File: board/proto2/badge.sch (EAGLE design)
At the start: 61 parts, among them IC1 TLV62569, J1 5051101092, J2 M05X2X1.27

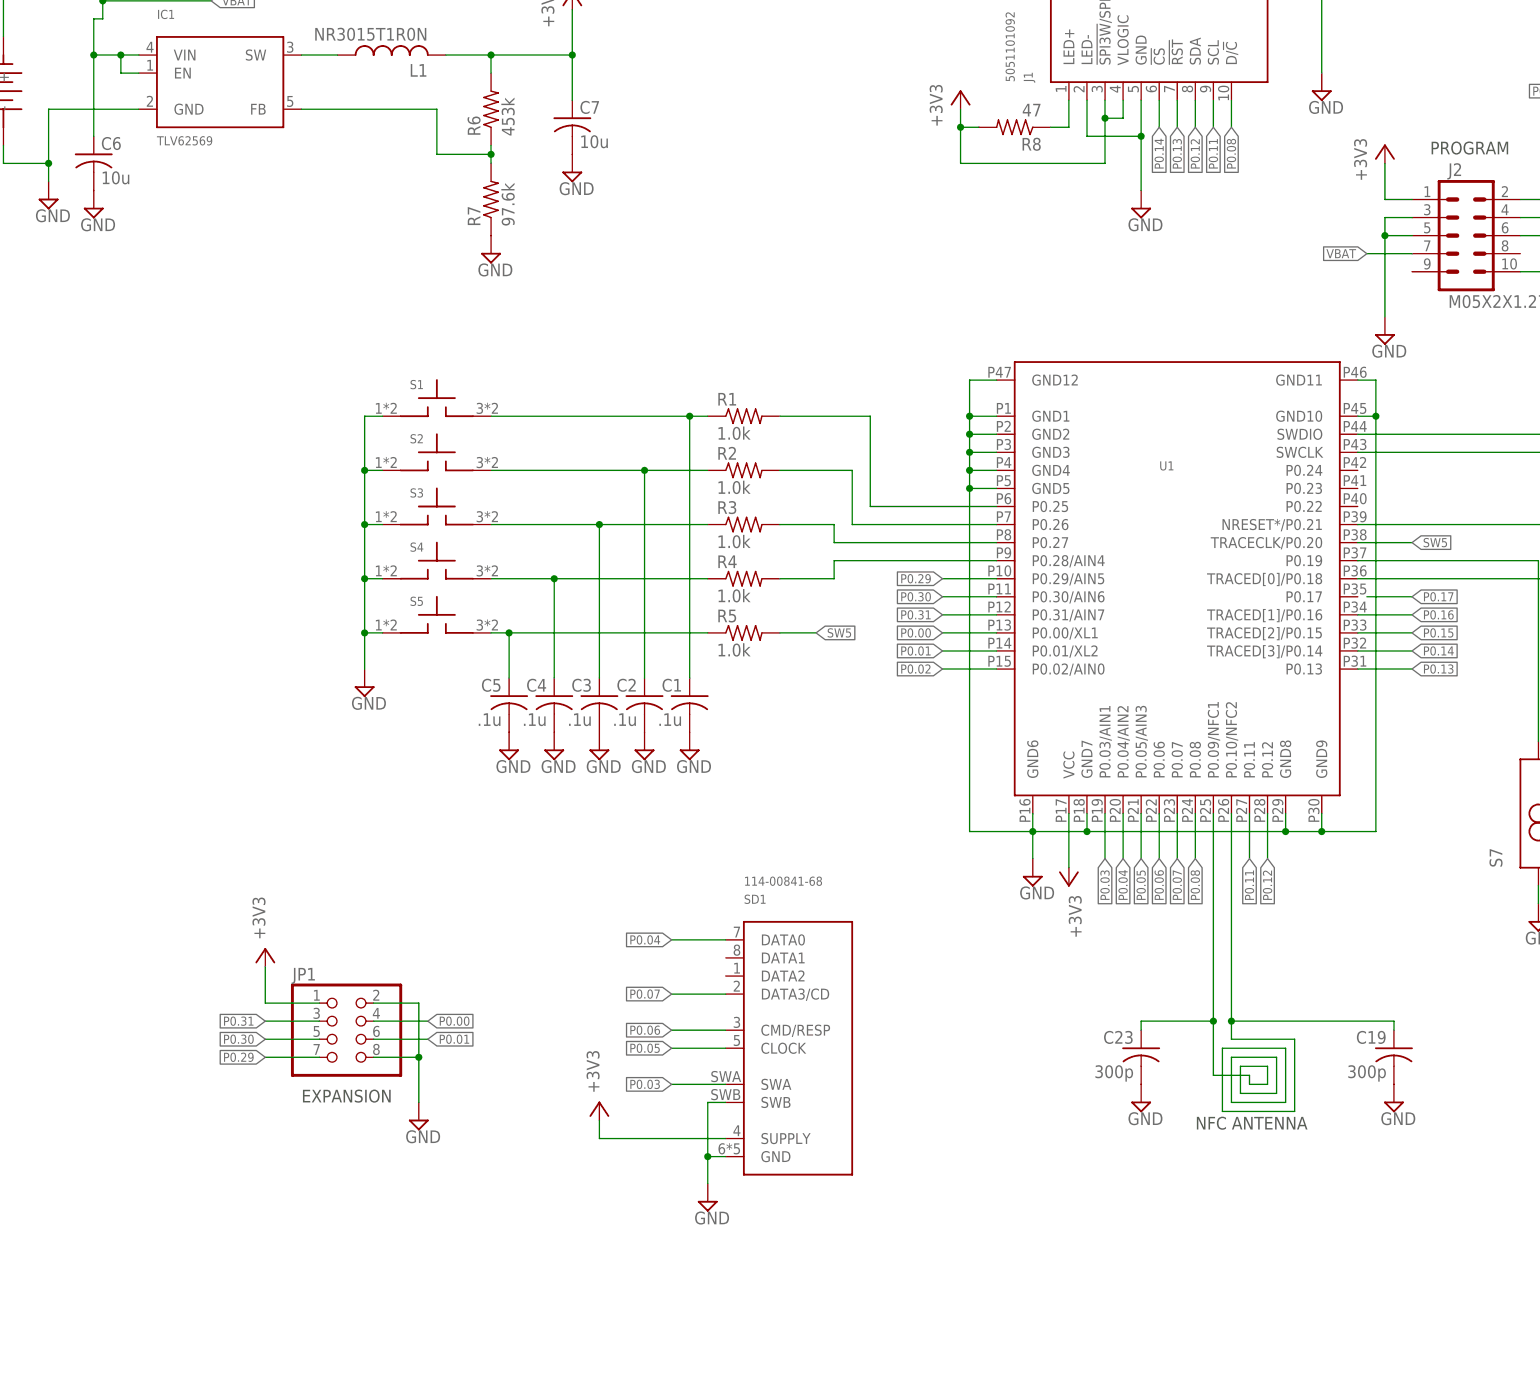
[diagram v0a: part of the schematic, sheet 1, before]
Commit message: add decoupling caps
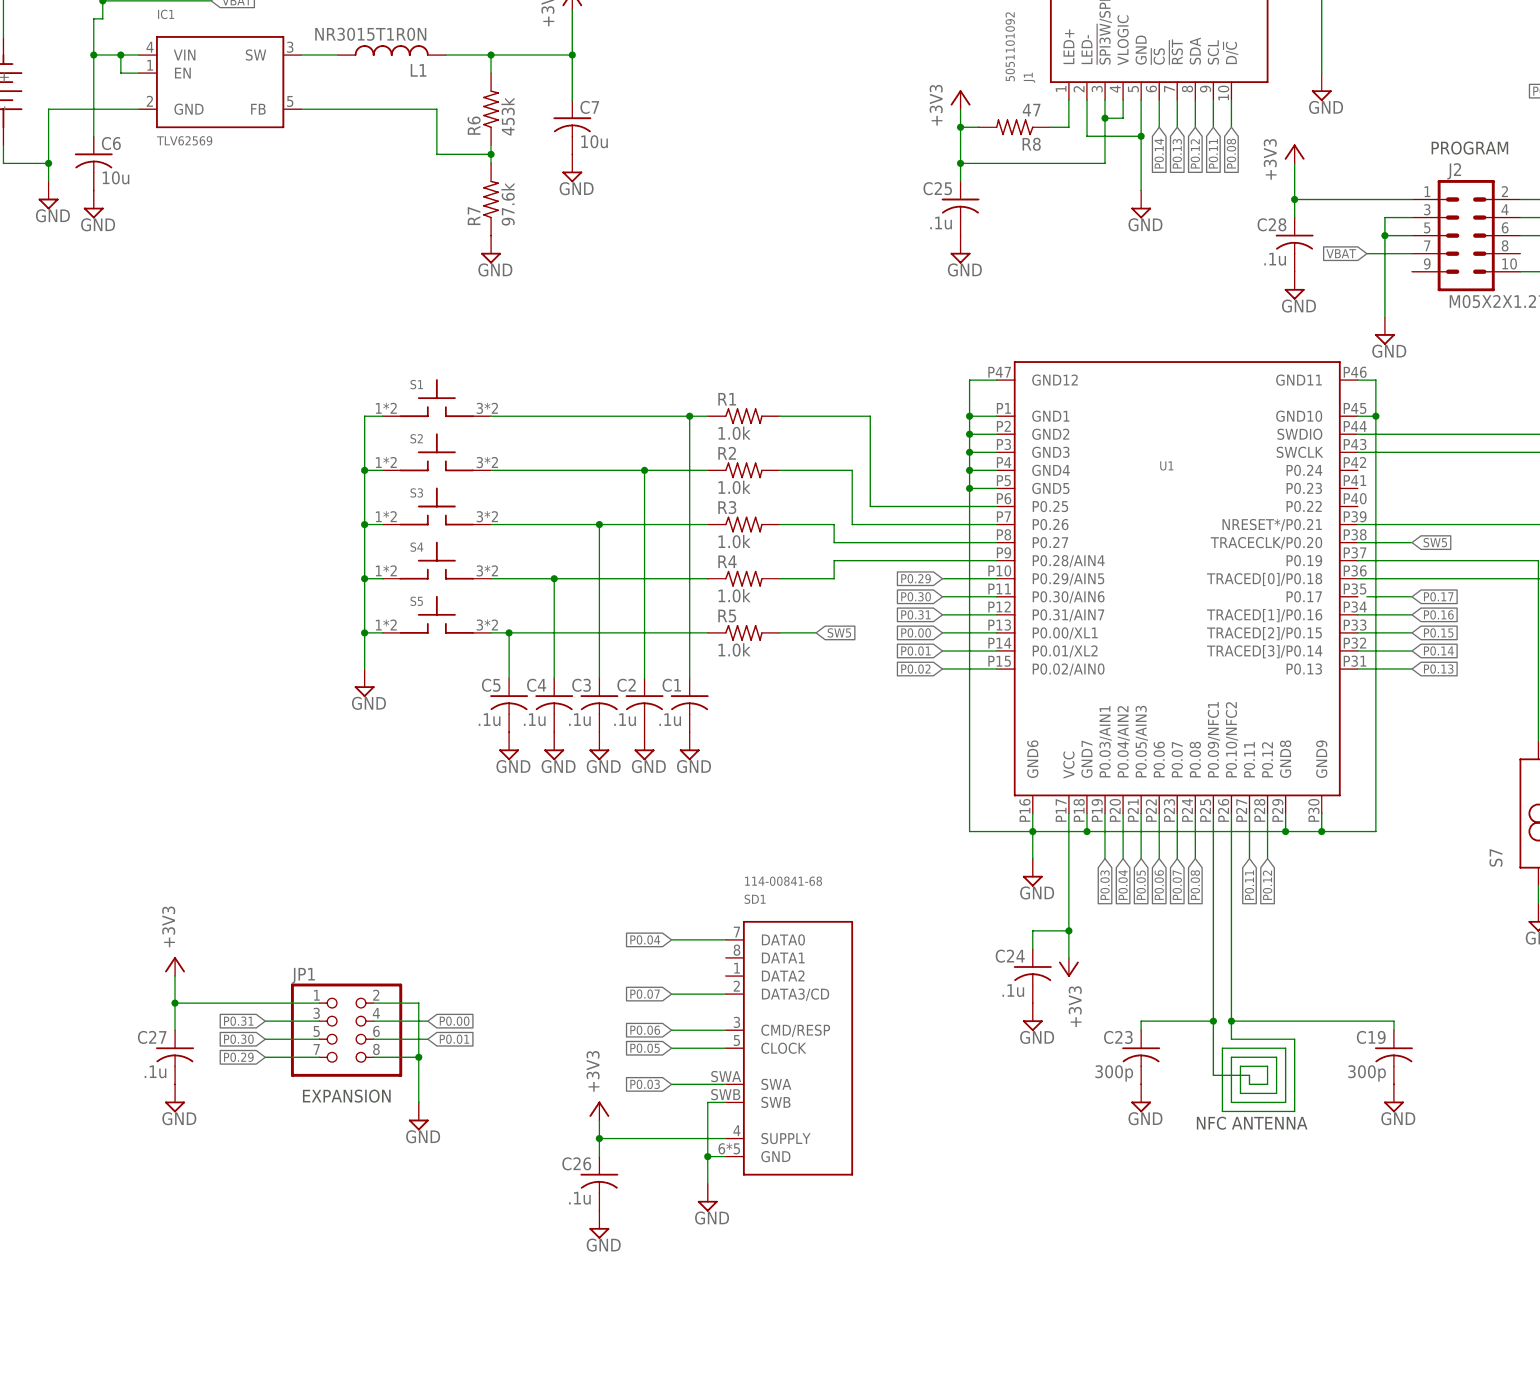
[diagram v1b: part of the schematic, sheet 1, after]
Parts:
- added C24, C25, C26, C27, C28: .1u, rcl:C-USC0402K
- C1, C10, C11, C12, C13, C14, C15, C16, C17, C18, C2, C20, C21, C22, C3, C4, C5, C8, C9: device rcl:C-USC0201 -> rcl:C-USC0402K
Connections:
- net +3V3: now also C24.1, C25.1, C26.1, C27.1, C28.1
- net GND: now also C24.2, C25.2, C26.2, C27.2, C28.2
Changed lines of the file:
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@@
 <part name="R4" library="rcl" deviceset="R-US_" device="R0603" value="1.0k"/>
 <part name="R5" library="rcl" deviceset="R-US_" device="R0603" value="1.0k"/>
-<part name="C1" library="rcl" deviceset="C-US" device="C0201" value=".1u"/>
-<part name="C2" library="rcl" deviceset="C-US" device="C0201" value=".1u"/>
-<part name="C3" library="rcl" deviceset="C-US" device="C0201" value=".1u"/>
-<part name="C4" library="rcl" deviceset="C-US" device="C0201" value=".1u"/>
-<part name="C5" library="rcl" deviceset="C-US" device="C0201" value=".1u"/>
+<part name="C1" library="rcl" deviceset="C-US" device="C0402K" value=".1u"/>
+<part name="C2" library="rcl" deviceset="C-US" device="C0402K" value=".1u"/>
+<part name="C3" library="rcl" deviceset="C-US" device="C0402K" value=".1u"/>
+<part name="C4" library="rcl" deviceset="C-US" device="C0402K" value=".1u"/>
+<part name="C5" library="rcl" deviceset="C-US" device="C0402K" value=".1u"/>
 <part name="+3V15" library="supply1" deviceset="+3V3" device=""/>
 <part name="SUPPLY1" library="supply2" deviceset="GND" device=""/>
@@
 <part name="+3V6" library="supply1" deviceset="+3V3" device=""/>
 <part name="R9" library="rcl" deviceset="R-US_" device="R0603" value="47"/>
-<part name="C8" library="rcl" deviceset="C-US" device="C0201" value=".1u"/>
-<part name="C9" library="rcl" deviceset="C-US" device="C0201" value=".1u"/>
-<part name="C10" library="rcl" deviceset="C-US" device="C0201" value=".1u"/>
-<part name="C11" library="rcl" deviceset="C-US" device="C0201" value=".1u"/>
-<part name="C12" library="rcl" deviceset="C-US" device="C0201" value=".1u"/>
-<part name="C13" library="rcl" deviceset="C-US" device="C0201" value=".1u"/>
-<part name="C14" library="rcl" deviceset="C-US" device="C0201" value=".1u"/>
-<part name="C15" library="rcl" deviceset="C-US" device="C0201" value=".1u"/>
+<part name="C8" library="rcl" deviceset="C-US" device="C0402K" value=".1u"/>
+<part name="C9" library="rcl" deviceset="C-US" device="C0402K" value=".1u"/>
+<part name="C10" library="rcl" deviceset="C-US" device="C0402K" value=".1u"/>
+<part name="C11" library="rcl" deviceset="C-US" device="C0402K" value=".1u"/>
+<part name="C12" library="rcl" deviceset="C-US" device="C0402K" value=".1u"/>
+<part name="C13" library="rcl" deviceset="C-US" device="C0402K" value=".1u"/>
+<part name="C14" library="rcl" deviceset="C-US" device="C0402K" value=".1u"/>
+<part name="C15" library="rcl" deviceset="C-US" device="C0402K" value=".1u"/>
 <part name="SUPPLY18" library="supply2" deviceset="GND" device=""/>
 <part name="SUPPLY19" library="supply2" deviceset="GND" device=""/>
@@
 <part name="SUPPLY24" library="supply2" deviceset="GND" device=""/>
 <part name="SUPPLY25" library="supply2" deviceset="GND" device=""/>
-<part name="C16" library="rcl" deviceset="C-US" device="C0201" value=".1u"/>
-<part name="C17" library="rcl" deviceset="C-US" device="C0201" value=".1u"/>
-<part name="C18" library="rcl" deviceset="C-US" device="C0201" value=".1u"/>
-<part name="C20" library="rcl" deviceset="C-US" device="C0201" value=".1u"/>
-<part name="C21" library="rcl" deviceset="C-US" device="C0201" value=".1u"/>
-<part name="C22" library="rcl" deviceset="C-US" device="C0201" value=".1u"/>
+<part name="C16" library="rcl" deviceset="C-US" device="C0402K" value=".1u"/>
+<part name="C17" library="rcl" deviceset="C-US" device="C0402K" value=".1u"/>
+<part name="C18" library="rcl" deviceset="C-US" device="C0402K" value=".1u"/>
+<part name="C20" library="rcl" deviceset="C-US" device="C0402K" value=".1u"/>
+<part name="C21" library="rcl" deviceset="C-US" device="C0402K" value=".1u"/>
+<part name="C22" library="rcl" deviceset="C-US" device="C0402K" value=".1u"/>
 <part name="SUPPLY26" library="supply2" deviceset="GND" device=""/>
 <part name="SUPPLY27" library="supply2" deviceset="GND" device=""/>
@@
 <part name="SUPPLY37" library="supply2" deviceset="GND" device=""/>
 <part name="+3V9" library="supply1" deviceset="+3V3" device=""/>
+<part name="C24" library="rcl" deviceset="C-US" device="C0402K" value=".1u"/>
+<part name="SUPPLY38" library="supply2" deviceset="GND" device=""/>
+<part name="C25" library="rcl" deviceset="C-US" device="C0402K" value=".1u"/>
+<part name="SUPPLY39" library="supply2" deviceset="GND" device=""/>
+<part name="C26" library="rcl" deviceset="C-US" device="C0402K" value=".1u"/>
+<part name="SUPPLY40" library="supply2" deviceset="GND" device=""/>
+<part name="C27" library="rcl" deviceset="C-US" device="C0402K" value=".1u"/>
+<part name="SUPPLY41" library="supply2" deviceset="GND" device=""/>
+<part name="SUPPLY42" library="supply2" deviceset="GND" device=""/>
+<part name="C28" library="rcl" deviceset="C-US" device="C0402K" value=".1u"/>
 </parts>
 <sheets>
@@
 <instance part="R7" gate="G$1" x="91.44" y="226.06" rot="R90"/>
 <instance part="SUPPLY11" gate="GND" x="91.44" y="218.44"/>
-<instance part="+3V1" gate="G$1" x="172.72" y="129.54" smashed="yes" rot="R180">
-<attribute name="VALUE" x="172.72" y="128.27" size="1.778" layer="96" rot="R270"/>
+<instance part="+3V1" gate="G$1" x="172.72" y="116.84" smashed="yes" rot="R180">
+<attribute name="VALUE" x="172.72" y="115.57" size="1.778" layer="96" rot="R270"/>
 </instance>
 <instance part="S6" gate="G$1" x="36.83" y="264.16" rot="R180"/>
@@
 </instance>
 <instance part="JP1" gate="A" x="69.85" y="107.95"/>
-<instance part="+3V8" gate="G$1" x="59.69" y="120.65" smashed="yes">
-<attribute name="VALUE" x="59.69" y="121.92" size="1.778" layer="96" rot="R90"/>
+<instance part="+3V8" gate="G$1" x="46.99" y="119.38" smashed="yes">
+<attribute name="VALUE" x="46.99" y="120.65" size="1.778" layer="96" rot="R90"/>
 </instance>
 <instance part="SUPPLY36" gate="GND" x="81.28" y="96.52"/>
 <instance part="J2" gate="G$1" x="228.6" y="220.98"/>
 <instance part="SUPPLY37" gate="GND" x="217.17" y="207.01"/>
-<instance part="+3V9" gate="G$1" x="217.17" y="233.68"/>
+<instance part="+3V9" gate="G$1" x="204.47" y="233.68"/>
+<instance part="C24" gate="G$1" x="167.64" y="118.11" rot="MR0"/>
+<instance part="SUPPLY38" gate="GND" x="167.64" y="110.49"/>
+<instance part="C25" gate="G$1" x="157.48" y="226.06" rot="MR0"/>
+<instance part="SUPPLY39" gate="GND" x="157.48" y="218.44"/>
+<instance part="C26" gate="G$1" x="106.68" y="88.9" rot="MR0"/>
+<instance part="SUPPLY40" gate="GND" x="106.68" y="81.28"/>
+<instance part="C27" gate="G$1" x="46.99" y="106.68" rot="MR0"/>
+<instance part="SUPPLY41" gate="GND" x="46.99" y="99.06"/>
+<instance part="SUPPLY42" gate="GND" x="204.47" y="213.36"/>
+<instance part="C28" gate="G$1" x="204.47" y="220.98" rot="MR0"/>
 </instances>
 <busses>
@@
 <pinref part="SUPPLY37" gate="GND" pin="GND"/>
 </segment>
+<segment>
+<pinref part="C24" gate="G$1" pin="2"/>
+<pinref part="SUPPLY38" gate="GND" pin="GND"/>
+</segment>
+<segment>
+<pinref part="C25" gate="G$1" pin="2"/>
+<pinref part="SUPPLY39" gate="GND" pin="GND"/>
+</segment>
+<segment>
+<pinref part="C26" gate="G$1" pin="2"/>
+<pinref part="SUPPLY40" gate="GND" pin="GND"/>
+</segment>
+<segment>
+<pinref part="C27" gate="G$1" pin="2"/>
+<pinref part="SUPPLY41" gate="GND" pin="GND"/>
+</segment>
+<segment>
+<pinref part="C28" gate="G$1" pin="2"/>
+<pinref part="SUPPLY42" gate="GND" pin="GND"/>
+</segment>
 </net>
 <net name="N$10" class="0">
@@
 <wire x1="36.83" y1="254" x2="52.07" y2="254" width="0.1524" layer="91"/>
 <junction x="36.83" y="254"/>
-<label x="52.07" y="254" size="1.27" layer="93" xref="yes"/>
+<label x="52.07" y="254" size="1.27" layer="91" xref="yes"/>
 </segment>
 <segment>
@@
 <segment>
 <pinref part="U1" gate="G$1" pin="VCC"/>
-<wire x1="172.72" y1="139.7" x2="172.72" y2="132.08" width="0.1524" layer="91"/>
+<wire x1="172.72" y1="139.7" x2="172.72" y2="123.19" width="0.1524" layer="91"/>
 <pinref part="+3V1" gate="G$1" pin="+3V3"/>
+<pinref part="C24" gate="G$1" pin="1"/>
+<wire x1="172.72" y1="123.19" x2="172.72" y2="119.38" width="0.1524" layer="91"/>
+<wire x1="167.64" y1="120.65" x2="167.64" y2="123.19" width="0.1524" layer="91"/>
+<wire x1="167.64" y1="123.19" x2="172.72" y2="123.19" width="0.1524" layer="91"/>
+<junction x="172.72" y="123.19"/>
 </segment>
 <segment>
@@
 <pinref part="J1" gate="G$1" pin="!SPI3W!/SPI4W"/>
 <pinref part="J1" gate="G$1" pin="VLOGIC"/>
+<pinref part="C25" gate="G$1" pin="1"/>
+<wire x1="157.48" y1="231.14" x2="157.48" y2="228.6" width="0.1524" layer="91"/>
+<junction x="157.48" y="231.14"/>
 </segment>
 <segment>
@@
 <pinref part="SD1" gate="G$1" pin="SUPPLY"/>
 <wire x1="106.68" y1="93.98" x2="124.46" y2="93.98" width="0.1524" layer="91"/>
+<pinref part="C26" gate="G$1" pin="1"/>
+<wire x1="106.68" y1="93.98" x2="106.68" y2="91.44" width="0.1524" layer="91"/>
+<junction x="106.68" y="93.98"/>
 </segment>
 <segment>
 <pinref part="JP1" gate="A" pin="1"/>
-<wire x1="67.31" y1="113.03" x2="59.69" y2="113.03" width="0.1524" layer="91"/>
-<wire x1="59.69" y1="113.03" x2="59.69" y2="118.11" width="0.1524" layer="91"/>
+<wire x1="67.31" y1="113.03" x2="46.99" y2="113.03" width="0.1524" layer="91"/>
+<wire x1="46.99" y1="113.03" x2="46.99" y2="116.84" width="0.1524" layer="91"/>
 <pinref part="+3V8" gate="G$1" pin="+3V3"/>
+<pinref part="C27" gate="G$1" pin="1"/>
+<wire x1="46.99" y1="113.03" x2="46.99" y2="109.22" width="0.1524" layer="91"/>
+<junction x="46.99" y="113.03"/>
 </segment>
 <segment>
 <pinref part="+3V9" gate="G$1" pin="+3V3"/>
 <pinref part="J2" gate="G$1" pin="1"/>
-<wire x1="217.17" y1="231.14" x2="217.17" y2="226.06" width="0.1524" layer="91"/>
-<wire x1="217.17" y1="226.06" x2="220.98" y2="226.06" width="0.1524" layer="91"/>
-</segment>
-</net>
+<wire x1="204.47" y1="231.14" x2="204.47" y2="226.06" width="0.1524" layer="91"/>
+<wire x1="204.47" y1="226.06" x2="220.98" y2="226.06" width="0.1524" layer="91"/>
+<pinref part="C28" gate="G$1" pin="1"/>
+<wire x1="204.47" y1="226.06" x2="204.47" y2="223.52" width="0.1524" layer="91"/>
+<junction x="204.47" y="226.06"/>
+</segment>
+</net>

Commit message: layout in process
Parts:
- added OLED1: CFAF128128B, badge:CFAF128128B
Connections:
- net N$10 renamed VIN
- net N$12 renamed FB
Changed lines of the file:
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@@
 <part name="SUPPLY42" library="supply2" deviceset="GND" device=""/>
 <part name="C28" library="rcl" deviceset="C-US" device="C0402K" value=".1u"/>
+<part name="OLED1" library="badge" deviceset="CFAF128128B" device=""/>
 </parts>
 <sheets>
@@
 <instance part="SUPPLY42" gate="GND" x="204.47" y="213.36"/>
 <instance part="C28" gate="G$1" x="204.47" y="220.98" rot="MR0"/>
+<instance part="OLED1" gate="G$1" x="128.27" y="241.3"/>
 </instances>
 <busses>
@@
 </segment>
 </net>
-<net name="N$10" class="0">
+<net name="VIN" class="0">
 <segment>
 <pinref part="B1" gate="G$1" pin="+"/>
@@
 </segment>
 </net>
-<net name="N$12" class="0">
+<net name="FB" class="0">
 <segment>
 <pinref part="R6" gate="G$1" pin="1"/>
